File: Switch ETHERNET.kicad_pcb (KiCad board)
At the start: 4 copper layers, 100 x 74.2 mm, 134 parts, among them J1 Conn_01x04, J2 RJ45_LED, J3 RJ45_LED, J4 RJ45_LED, J5 RJ45_LED, J6 RJ45_LED, J7 Jack-DC, J8 Conn_01x04, Q1 SI2301-ZE, SW1 SW_Push, U1 RTL8367N-VB-CG, U2 TPS563201, U3 TPS563201, Y1 25MHz

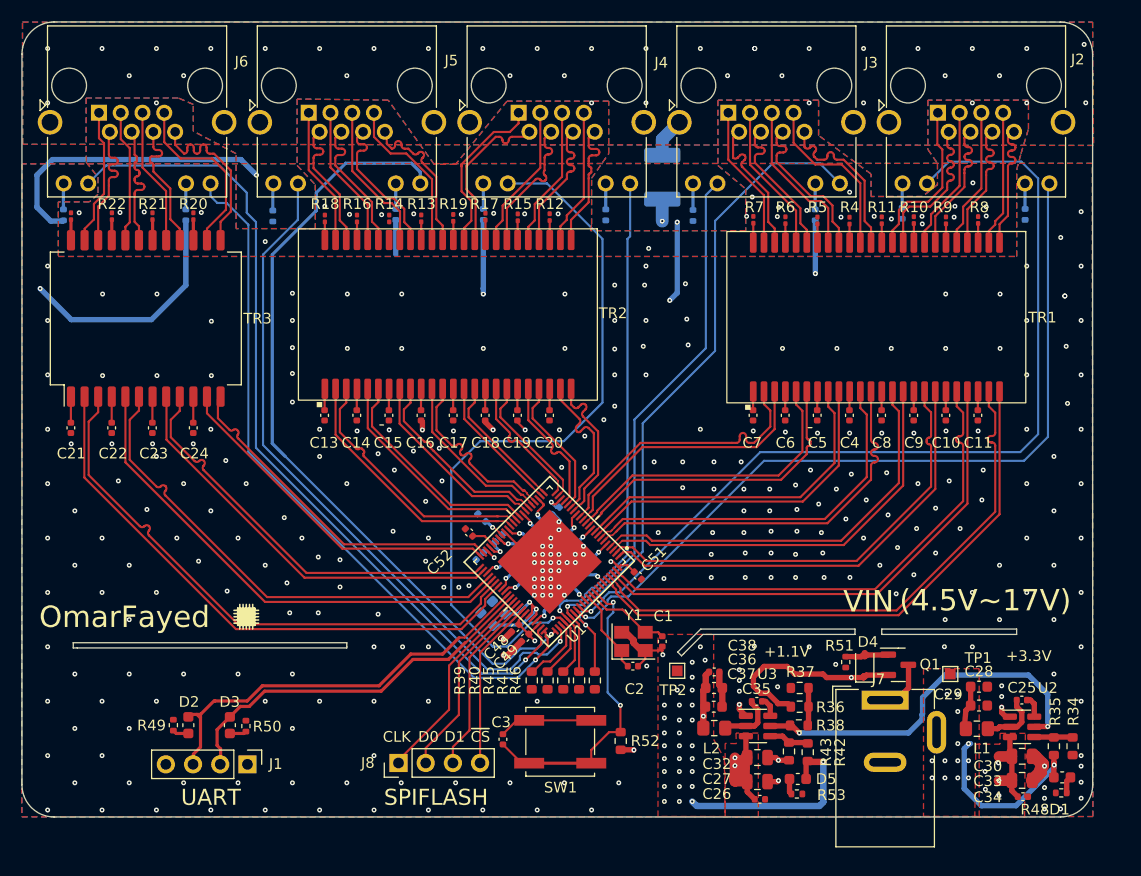
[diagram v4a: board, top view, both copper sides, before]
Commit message: Added Photos of PCB in real life
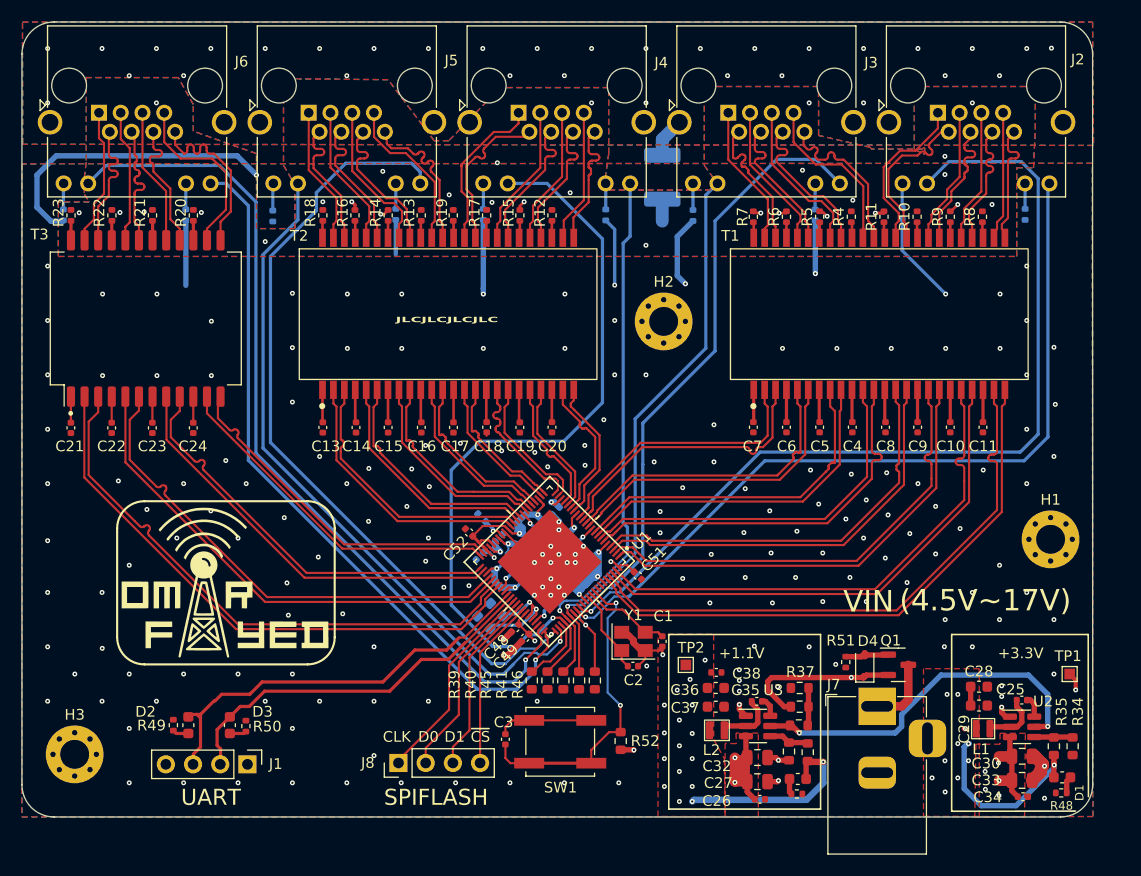
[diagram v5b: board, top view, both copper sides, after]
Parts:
- removed TR1, TR2: 350uH, H4801G:H4801G
- added G***: LOGO, KiCad:Logo +, F.Cu at (169.1, 78.1)
- added H1: MountingHole, MountingHole:MountingHole_2.7mm_M2.5_Pad_Via, F.Cu at (246.1, 74.1)
- added H2: MountingHole, MountingHole:MountingHole_2.7mm_M2.5_Pad_Via, F.Cu at (209.9, 53.7)
- added H3: MountingHole, MountingHole:MountingHole_2.7mm_M2.5_Pad_Via, F.Cu at (154.9, 94.2)
- added T1: 350uH, Components:H4801G, F.Cu at (216.2, 46.9)
- added T2: 350uH, Components:H4801G, F.Cu at (175.9, 46.9)
- J7: value Jack-DC -> Barrel_Jack_Switch; footprint Connector_BarrelJack:BarrelJack_Wuerth_6941xx301002 -> Connector_BarrelJack:BarrelJack_Horizontal
- R10, R11, R12, R13, R14, R15, R16, R17, R18, R19, R20, R21, R22, R23, R4, R5, R6, R7, R8, R9: footprint Resistor_SMD:R_0201_0603Metric -> Resistor_SMD:R_0402_1005Metric
- moved TP1 11.2 mm to (247.8, 86.7)
- moved L1 1.80 mm to (240.8, 92.6)
- moved L2 1.70 mm to (216.0, 92.8)
- moved C11 1.21 mm to (239.8, 63.6)
- moved C10 1.19 mm to (236.7, 63.6)
- moved C8 1.17 mm to (230.7, 63.6)
- moved C9 1.17 mm to (233.7, 63.6)
- moved C19 1.15 mm to (196.5, 63.6)
- moved C13 1.14 mm to (178.1, 63.6)
- moved C4 1.14 mm to (227.6, 63.6)
- moved C20 1.13 mm to (199.5, 63.6)
- moved C5 1.13 mm to (224.5, 63.6)
- moved C15 1.13 mm to (184.2, 63.6)
- moved C14 1.13 mm to (181.2, 63.6)
- moved C16 1.13 mm to (187.3, 63.6)
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- renumbered TR3 to T3
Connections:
- C31 pad 1: +3.3V -> +3.3VA
- C39 pad 1: +3.3V -> +3.3VA
- C41 pad 1: +3.3V -> +3.3VA
- C42 pad 1: +3.3V -> +3.3VA
- C43 pad 1: +1V1 -> +1.1VA
- C44 pad 1: +3.3V -> +3.3VA
- C45 pad 1: +1V1 -> +1.1VA
- C46 pad 1: +1V1 -> +1.1VA
- C47 pad 1: +1V1 -> +1.1VA
- C50 pad 1: +1V1 -> +1.1VA
- C51 pad 1: +1V1 -> +1.1VA
- C52 pad 1: +3.3V -> +3.3VA
- C54 pad 1: +3.3V -> +3.3VA
- C55 pad 1: +3.3V -> +3.3VA
- C56 pad 1: +1V1 -> +1.1VA
- U1 pad 10: +1V1 -> +1.1VA
- U1 pad 20: +1V1 -> +1.1VA
- U1 pad 25: +3.3V -> +3.3VA
- U1 pad 30: +1V1 -> +1.1VA
- U1 pad 35: +3.3V -> +3.3VA
- U1 pad 38: +1V1 -> +1.1VA
- U1 pad 40: +3.3V -> +3.3VA
- U1 pad 42: +3.3V -> +3.3VA
- U1 pad 47: +1V1 -> +1.1VA
- U1 pad 5: +3.3V -> +3.3VA
- U1 pad 52: +3.3V -> +3.3VA
- U1 pad 53: +1V1 -> +1.1VA
- U1 pad 77: +3.3V -> +3.3VA
- U1 pad 83: +3.3V -> +3.3VA
- U1 pad 88: +1V1 -> +1.1VA
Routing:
- net +3.3VA: track 0.00 -> 84.6 mm, vias 0 -> 7
- net +1V1: track 114.1 -> 48.0 mm, vias 41 -> 20
- net GND: track 159.3 -> 126.9 mm, vias 307 -> 193
- net +3.3V: track 96.3 -> 128.0 mm, vias 23 -> 14
- net +1.1VA: track 0.00 -> 20.7 mm, vias 0 -> 7
- net HV_CHASIS: track 15.4 -> 22.4 mm, vias 34 -> 29
- net P4LED1: track 66.6 -> 68.9 mm
- net P3MDIA_P: track 17.9 -> 16.2 mm
- net VDC: track 4.83 -> 6.45 mm
- net Net-(T2-0CTT3): track 0.00 -> 1.59 mm
- net P4LED0: track 79.0 -> 80.5 mm
- net P1MDID_P: track 25.7 -> 27.1 mm
- net VCC: track 99.6 -> 98.3 mm
- net P2MDIC_P: track 12.8 -> 14.1 mm
- net Net-(T1-1CT1): track 1.76 -> 3.04 mm
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- added copper zone on In2.Cu, net +1.1VA
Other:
- outline, holes or cut-outs redrawn
- board text added: "5-Port Gigabit ETHERNET Switch Version 1.0 14/6/2023"
- board text added: "JLCJLCJLCJLC"
- board text removed: "4/6/23"
- board text removed: "OmarFayed"
